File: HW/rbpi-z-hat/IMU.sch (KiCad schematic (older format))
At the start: 11 parts, among them U1 MPU-9250

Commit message: Commit...
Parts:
- removed C1, C5: 100nF, Capacitor_SMD:C_0603_1608Metric, symbol Device:C
- removed C3: 10nF, Capacitor_SMD:C_0603_1608Metric, symbol Device:C
- removed C6: 22uF/10V, Capacitor_SMD:C_1206_3216Metric, symbol Device:C
- removed C7: 0.1uF, Capacitor_SMD:C_0603_1608Metric, symbol Device:C
- removed L1, L4: Ferrite_Bead, Inductor_SMD:L_0603_1608Metric, symbol Device:Ferrite_Bead
- removed R1: 120, Resistor_SMD:R_0603_1608Metric, symbol Device:R
- removed R2, R3: 10K, Resistor_SMD:R_0603_1608Metric, symbol Device:R
- removed U1: MPU-9250, Package_DFN_QFN:QFN-24-1EP_3x3mm_P0.4mm_EP1.75x1.6mm, symbol Sensor_Motion:MPU-9250
- added C22: 100nF, Capacitor_SMD:C_0603_1608Metric, symbol Device:C
- added L10, L11: Ferrite_Bead, Inductor_SMD:L_0603_1608Metric, symbol Device:Ferrite_Bead
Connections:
- new net IMU_FGND: L11.2
- new net IMU_GND: C22.2, L11.1
- new net IMU_VIN: C22.1, L10.1
- new net MIC5504_IMU/MIC_VIN: L10.2
- no-connect marks 2 -> 0
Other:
- note removed: "CL31B226KPHNNNE"

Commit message: Commit
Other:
- moved on the sheet: C22, L10, L11
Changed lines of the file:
@@
 L Device:Ferrite_Bead L?
 U 1 1 5EE0B780
-P 3850 6650
+P 3550 6650
 AR Path="/5ED663F7/5EE0B780" Ref="L?"  Part="1"
 AR Path="/5EF65A4D/5EF663FB/5EE0B780" Ref="L?"  Part="1"
 AR Path="/5EF65A4D/5EE0B780" Ref="L?"  Part="1"
 AR Path="/5EE06F22/5EE0B780" Ref="L10"  Part="1"
-F 0 "L10" V 4100 6650 50  0000 C CNN
-F 1 "Ferrite_Bead" V 4000 6650 50  0000 C CNN
-F 2 "Inductor_SMD:L_0603_1608Metric" V 3780 6650 50  0001 C CNN
-F 3 "~" H 3850 6650 50  0001 C CNN
-	1    3850 6650
+F 0 "L10" V 3800 6650 50  0000 C CNN
+F 1 "Ferrite_Bead" V 3700 6650 50  0000 C CNN
+F 2 "Inductor_SMD:L_0603_1608Metric" V 3480 6650 50  0001 C CNN
+F 3 "~" H 3550 6650 50  0001 C CNN
+	1    3550 6650
 	0    -1   -1   0
 $EndComp
@@
 L Device:C C?
 U 1 1 5EE0B786
-P 3500 7200
+P 3200 7200
 AR Path="/5ED663F7/5EE0B786" Ref="C?"  Part="1"
 AR Path="/5EF65A4D/5EF663FB/5EE0B786" Ref="C?"  Part="1"
 AR Path="/5EF65A4D/5EE0B786" Ref="C?"  Part="1"
 AR Path="/5EE06F22/5EE0B786" Ref="C22"  Part="1"
-F 0 "C22" H 3550 7300 50  0000 L CNN
-F 1 "100nF" H 3550 7100 50  0000 L CNN
-F 2 "Capacitor_SMD:C_0603_1608Metric" H 3538 7050 50  0001 C CNN
-F 3 "" H 3500 7200 50  0001 C CNN
-	1    3500 7200
+F 0 "C22" H 3250 7300 50  0000 L CNN
+F 1 "100nF" H 3250 7100 50  0000 L CNN
+F 2 "Capacitor_SMD:C_0603_1608Metric" H 3238 7050 50  0001 C CNN
+F 3 "" H 3200 7200 50  0001 C CNN
+	1    3200 7200
 	1    0    0    -1
 $EndComp
 Wire Wire Line
-	3250 6650 3500 6650
-Wire Wire Line
-	3700 6650 3500 6650
-Connection ~ 3500 6650
-Wire Wire Line
-	3500 6650 3500 7050
-Wire Wire Line
-	3500 7350 3500 7750
+	2950 6650 3200 6650
+Wire Wire Line
+	3400 6650 3200 6650
+Connection ~ 3200 6650
+Wire Wire Line
+	3200 6650 3200 7050
+Wire Wire Line
+	3200 7350 3200 7750
 $Comp
 L Device:Ferrite_Bead L?
 U 1 1 5EE0B798
-P 3850 7750
+P 3550 7750
 AR Path="/5ED663F7/5EE0B798" Ref="L?"  Part="1"
 AR Path="/5EF65A4D/5EF663FB/5EE0B798" Ref="L?"  Part="1"
 AR Path="/5EF65A4D/5EE0B798" Ref="L?"  Part="1"
 AR Path="/5EE06F22/5EE0B798" Ref="L11"  Part="1"
-F 0 "L11" V 4050 7750 50  0000 C CNN
-F 1 "Ferrite_Bead" V 3700 7750 50  0000 C CNN
-F 2 "Inductor_SMD:L_0603_1608Metric" V 3780 7750 50  0001 C CNN
-F 3 "~" H 3850 7750 50  0001 C CNN
-	1    3850 7750
+F 0 "L11" V 3750 7750 50  0000 C CNN
+F 1 "Ferrite_Bead" V 3400 7750 50  0000 C CNN
+F 2 "Inductor_SMD:L_0603_1608Metric" V 3480 7750 50  0001 C CNN
+F 3 "~" H 3550 7750 50  0001 C CNN
+	1    3550 7750
 	0    -1   -1   0
 $EndComp
 Wire Wire Line
-	3700 7750 3500 7750
-Connection ~ 3500 7750
-Wire Wire Line
-	3500 7750 3250 7750
+	3400 7750 3200 7750
+Connection ~ 3200 7750
+Wire Wire Line
+	3200 7750 2950 7750
 Text Label 5550 6650 2    50   ~ 0
 IMU_VDD
@@
 IMU_VDD
 Wire Wire Line
-	4000 6650 4200 6650
-Wire Wire Line
-	4000 7750 4550 7750
-Text HLabel 3250 6650 0    50   Input ~ 0
+	3700 6650 4200 6650
+Wire Wire Line
+	3700 7750 4150 7750
+Text HLabel 2950 6650 0    50   Input ~ 0
 IMU_VIN
-Text HLabel 3250 7750 0    50   Input ~ 0
+Text HLabel 2950 7750 0    50   Input ~ 0
 IMU_GND
 Wire Wire Line
@@
 Text HLabel 2850 4100 0    50   Input ~ 0
 MPU_INT
+Wire Wire Line
+	4150 7750 4150 6850
+Wire Wire Line
+	4150 6850 4200 6850
+Connection ~ 4150 7750
+Wire Wire Line
+	4150 7750 4550 7750
+Wire Wire Line
+	4200 2650 4050 2650
+Wire Wire Line
+	4200 2750 4050 2750
+Wire Wire Line
+	4200 2850 4050 2850
+Wire Wire Line
+	4200 2950 4050 2950
+Wire Wire Line
+	4200 3050 4050 3050
+Wire Wire Line
+	4200 5200 3750 5200
+Wire Wire Line
+	4200 5300 3750 5300
+Text HLabel 3750 5200 0    50   Output ~ 0
+ICM_INT1
+Text HLabel 3750 5300 0    50   Output ~ 0
+ICM_INT2
+Text HLabel 4050 2650 0    50   Output ~ 0
+LSM_DEN
+Text HLabel 4050 2750 0    50   Output ~ 0
+LSM_INT1
+Text HLabel 4050 2850 0    50   Output ~ 0
+LSM_INT2
+Text HLabel 4050 2950 0    50   Output ~ 0
+LSM_INT3
+Text HLabel 4050 3050 0    50   Output ~ 0
+LSM_INT4
+Wire Wire Line
+	4200 6750 4150 6750
+Text HLabel 4150 6750 0    50   Input ~ 0
+SENS_EN
 $EndSCHEMATC

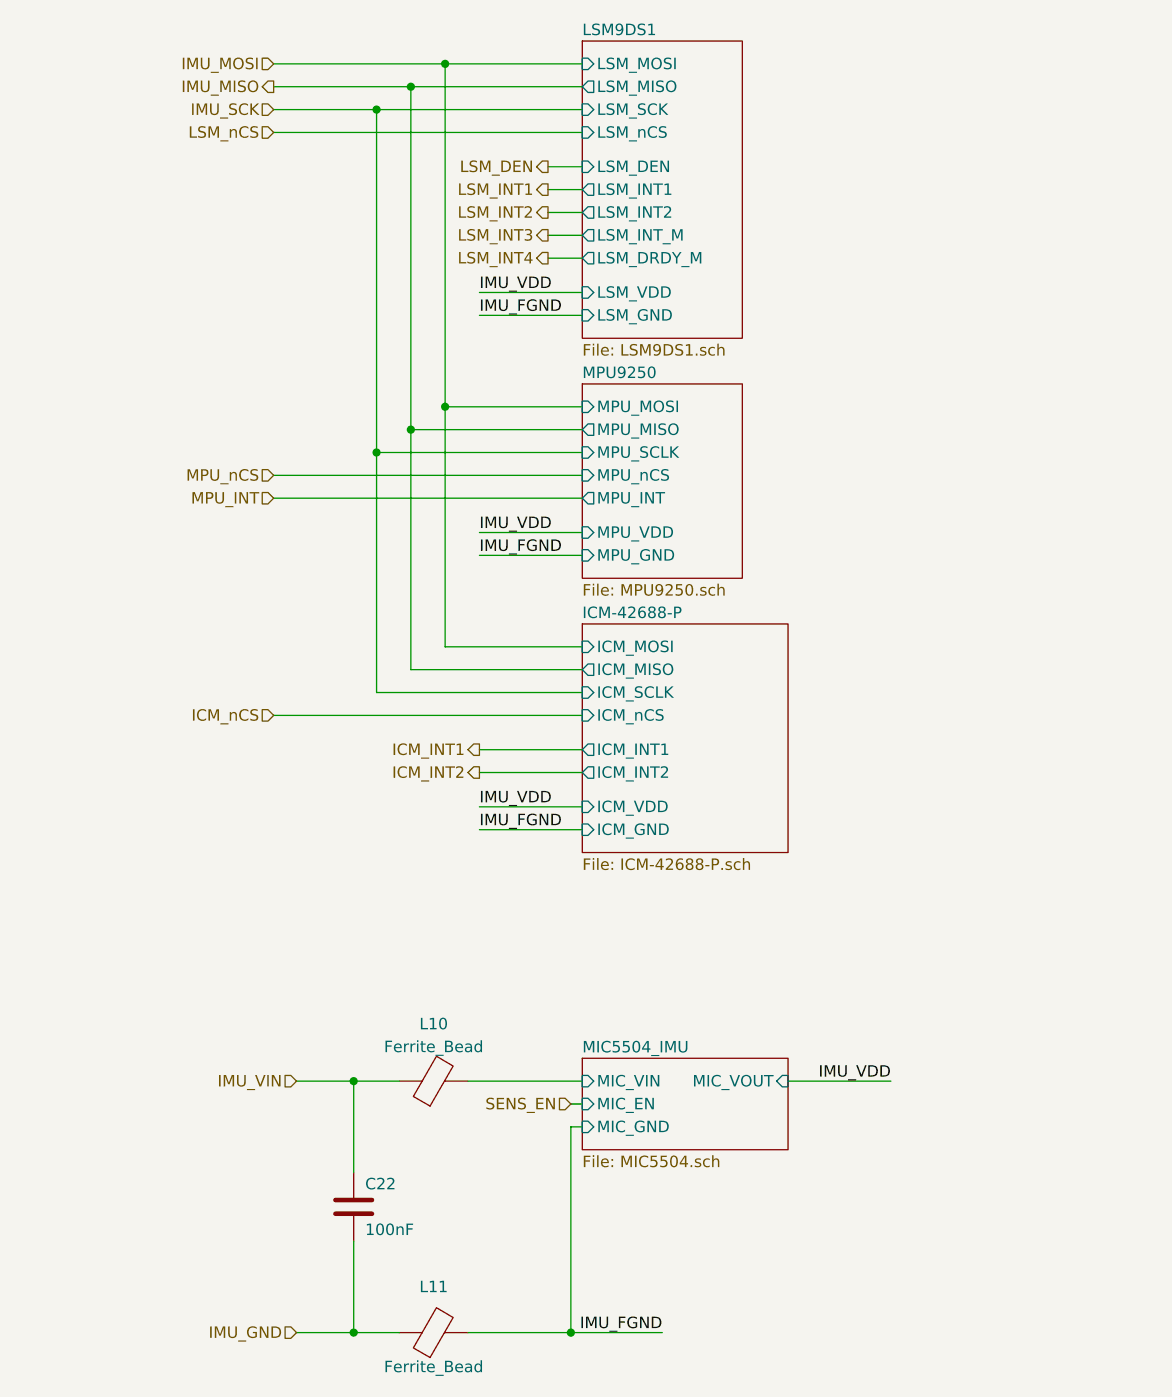
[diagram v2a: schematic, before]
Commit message: Removed MPU-9250
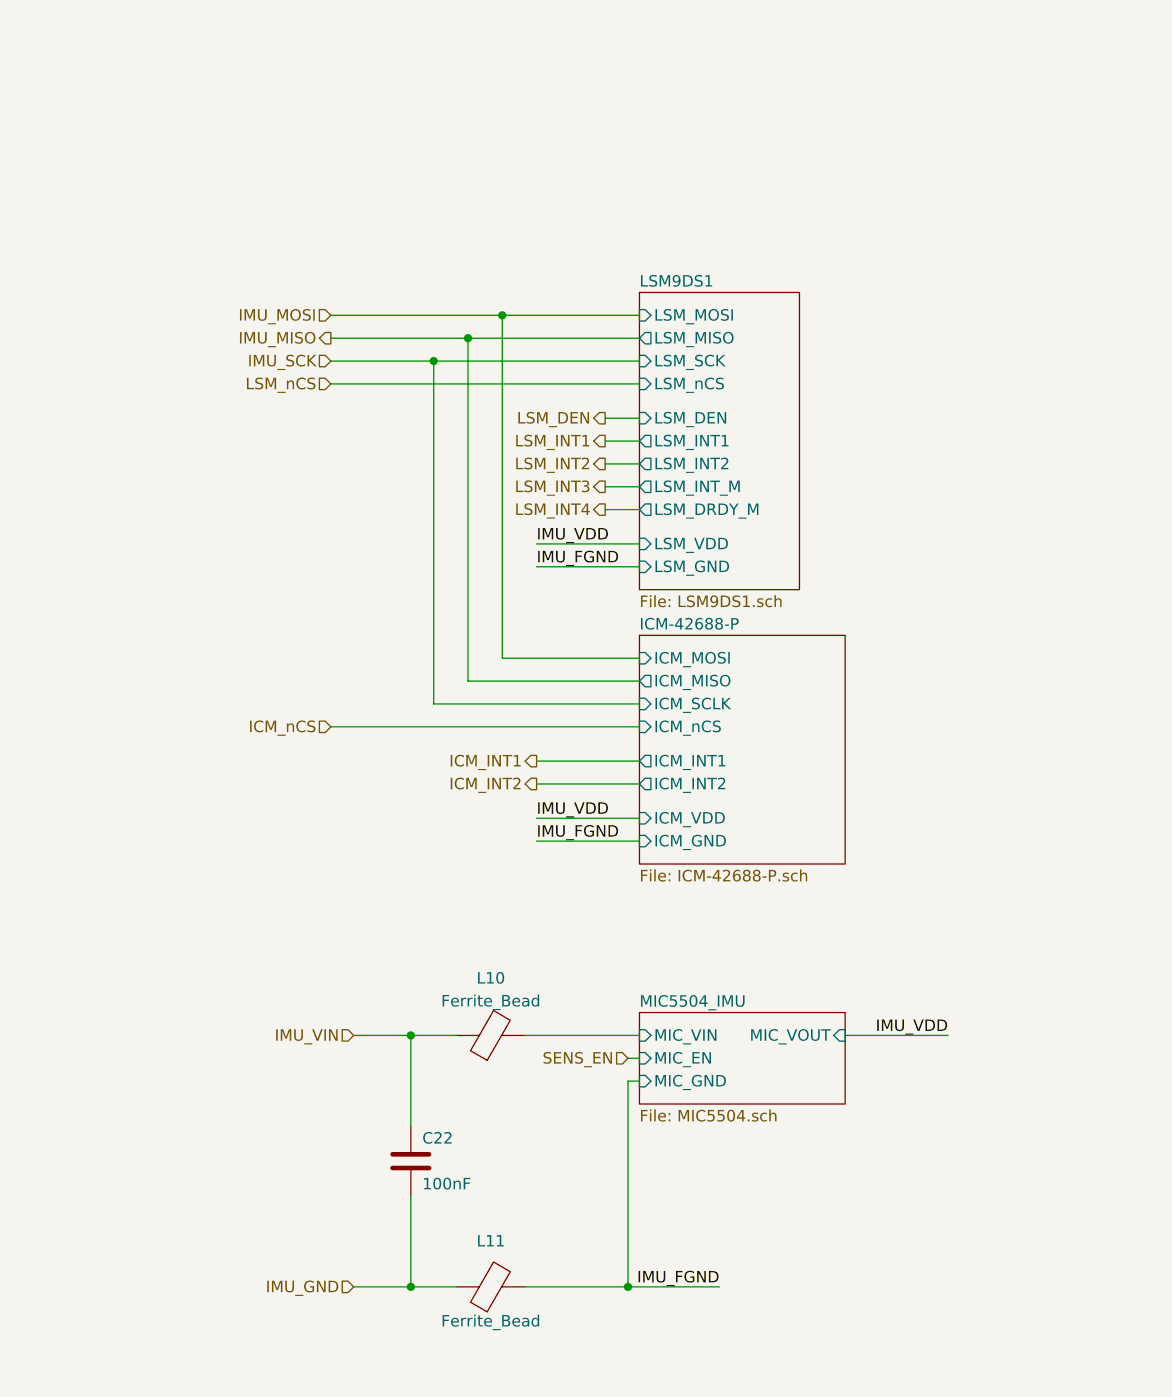
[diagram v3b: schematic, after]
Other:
- moved on the sheet: C22, L10, L11

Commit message: Commit
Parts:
- removed C22: 100nF, Capacitor_SMD:C_0603_1608Metric, symbol Device:C
- removed L10, L11: Ferrite_Bead, Inductor_SMD:L_0603_1608Metric, symbol Device:Ferrite_Bead
- added C?: 22uF/10V, Capacitor_SMD:C_1206_3216Metric, symbol Device:C
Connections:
- net IMU_GND: now also C?.2
- net IMU_VIN: now also C?.1
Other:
- note added: "CL31B226KPHNNNE"
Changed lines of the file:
@@
 $Descr A4 8268 11693 portrait
 encoding utf-8
-Sheet 14 17
+Sheet 13 17
 Title ""
 Date ""
@@
 $EndSheet
 Wire Wire Line
-	5800 6450 5350 6450
-$Comp
-L Device:Ferrite_Bead L?
-U 1 1 5EE0B780
-P 3800 6450
-AR Path="/5ED663F7/5EE0B780" Ref="L?"  Part="1"
-AR Path="/5EF65A4D/5EF663FB/5EE0B780" Ref="L?"  Part="1"
-AR Path="/5EF65A4D/5EE0B780" Ref="L?"  Part="1"
-AR Path="/5EE06F22/5EE0B780" Ref="L10"  Part="1"
-F 0 "L10" V 4050 6450 50  0000 C CNN
-F 1 "Ferrite_Bead" V 3950 6450 50  0000 C CNN
-F 2 "Inductor_SMD:L_0603_1608Metric" V 3730 6450 50  0001 C CNN
-F 3 "~" H 3800 6450 50  0001 C CNN
-	1    3800 6450
-	0    -1   -1   0
-$EndComp
-$Comp
-L Device:C C?
-U 1 1 5EE0B786
-P 3450 7000
-AR Path="/5ED663F7/5EE0B786" Ref="C?"  Part="1"
-AR Path="/5EF65A4D/5EF663FB/5EE0B786" Ref="C?"  Part="1"
-AR Path="/5EF65A4D/5EE0B786" Ref="C?"  Part="1"
-AR Path="/5EE06F22/5EE0B786" Ref="C22"  Part="1"
-F 0 "C22" H 3500 7100 50  0000 L CNN
-F 1 "100nF" H 3500 6900 50  0000 L CNN
-F 2 "Capacitor_SMD:C_0603_1608Metric" H 3488 6850 50  0001 C CNN
-F 3 "" H 3450 7000 50  0001 C CNN
-	1    3450 7000
-	1    0    0    -1
-$EndComp
-Wire Wire Line
-	3200 6450 3450 6450
-Wire Wire Line
-	3650 6450 3450 6450
-Connection ~ 3450 6450
-Wire Wire Line
-	3450 6450 3450 6850
-Wire Wire Line
-	3450 7150 3450 7550
-$Comp
-L Device:Ferrite_Bead L?
-U 1 1 5EE0B798
-P 3800 7550
-AR Path="/5ED663F7/5EE0B798" Ref="L?"  Part="1"
-AR Path="/5EF65A4D/5EF663FB/5EE0B798" Ref="L?"  Part="1"
-AR Path="/5EF65A4D/5EE0B798" Ref="L?"  Part="1"
-AR Path="/5EE06F22/5EE0B798" Ref="L11"  Part="1"
-F 0 "L11" V 4000 7550 50  0000 C CNN
-F 1 "Ferrite_Bead" V 3650 7550 50  0000 C CNN
-F 2 "Inductor_SMD:L_0603_1608Metric" V 3730 7550 50  0001 C CNN
-F 3 "~" H 3800 7550 50  0001 C CNN
-	1    3800 7550
-	0    -1   -1   0
-$EndComp
-Wire Wire Line
-	3650 7550 3450 7550
-Connection ~ 3450 7550
-Wire Wire Line
-	3450 7550 3200 7550
-Text Label 5800 6450 2    50   ~ 0
-IMU_VDD
-Text Label 4800 7550 2    50   ~ 0
-IMU_FGND
-$Sheet
-S 4450 6350 900  400
-U 5EE2A025
-F0 "MIC5504_IMU" 50
-F1 "MIC5504.sch" 50
-F2 "MIC_EN" I L 4450 6550 50
-F3 "MIC_VIN" I L 4450 6450 50
-F4 "MIC_VOUT" I R 5350 6450 50
-F5 "MIC_GND" I L 4450 6650 50
-$EndSheet
-Wire Wire Line
 	4000 5600 4450 5600
 Text Label 4000 5600 0    50   ~ 0
@@
 Text Label 4000 5500 0    50   ~ 0
 IMU_VDD
-Wire Wire Line
-	3950 6450 4450 6450
-Wire Wire Line
-	3950 7550 4400 7550
-Text HLabel 3200 6450 0    50   Input ~ 0
-IMU_VIN
-Text HLabel 3200 7550 0    50   Input ~ 0
-IMU_GND
 Wire Wire Line
 	4000 4400 4450 4400
@@
 ICM_nCS
 Wire Wire Line
-	4400 7550 4400 6650
-Wire Wire Line
-	4400 6650 4450 6650
-Connection ~ 4400 7550
-Wire Wire Line
-	4400 7550 4800 7550
-Wire Wire Line
 	4450 3750 4300 3750
 Wire Wire Line
@@
 LSM_INT4
 Wire Wire Line
-	4450 6550 4400 6550
-Text HLabel 4400 6550 0    50   Input ~ 0
-SENS_EN
-Wire Wire Line
 	3850 3300 3850 4800
 Wire Wire Line
@@
 Wire Wire Line
 	3550 3500 3550 5000
+Wire Wire Line
+	3600 6400 3600 6650
+Wire Wire Line
+	3600 7200 3600 6950
+$Comp
+L Device:C C?
+U 1 1 5EE70328
+P 3600 6800
+AR Path="/5ED663F7/5EE70328" Ref="C?"  Part="1"
+AR Path="/5EF65A4D/5EF663FB/5EE70328" Ref="C?"  Part="1"
+AR Path="/5EF65A4D/5EE70328" Ref="C?"  Part="1"
+AR Path="/5EDADA57/5EE70328" Ref="C?"  Part="1"
+AR Path="/5EF65A4D/5EE0D50D/5EE70328" Ref="C?"  Part="1"
+AR Path="/5EE06F22/5EE2A025/5EE70328" Ref="C?"  Part="1"
+AR Path="/5EE06F22/5EE70328" Ref="C?"  Part="1"
+F 0 "C?" H 3450 6900 50  0000 L CNN
+F 1 "22uF/10V" H 3200 6700 50  0000 L CNN
+F 2 "Capacitor_SMD:C_1206_3216Metric" H 3638 6650 50  0001 C CNN
+F 3 "" H 3600 6800 50  0001 C CNN
+F 4 "https://www.terraelectronica.ru/product/1641498" H 3600 6800 50  0001 C CNN "URL"
+	1    3600 6800
+	-1   0    0    -1
+$EndComp
+Text Notes 3500 7200 1    50   ~ 0
+CL31B226KPHNNNE
+Connection ~ 3600 6400
+Text HLabel 3100 6400 0    50   Input ~ 0
+IMU_VIN
+Wire Wire Line
+	3100 6400 3600 6400
+Text HLabel 3100 7200 0    50   Input ~ 0
+IMU_GND
+Wire Wire Line
+	3100 7200 3600 7200
+Text Label 4250 6400 2    50   ~ 0
+IMU_VDD
+Wire Wire Line
+	3600 6400 4250 6400
+Text Label 4250 7200 2    50   ~ 0
+IMU_FGND
+Wire Wire Line
+	3600 7200 4250 7200
+Connection ~ 3600 7200
 $EndSCHEMATC

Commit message: Commit
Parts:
- gave numbers to parts that had none: 1
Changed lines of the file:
@@
 AR Path="/5EF65A4D/5EE0D50D/5EE70328" Ref="C?"  Part="1"
 AR Path="/5EE06F22/5EE2A025/5EE70328" Ref="C?"  Part="1"
-AR Path="/5EE06F22/5EE70328" Ref="C?"  Part="1"
-F 0 "C?" H 3450 6900 50  0000 L CNN
+AR Path="/5EE06F22/5EE70328" Ref="C3"  Part="1"
+F 0 "C3" H 3450 6900 50  0000 L CNN
 F 1 "22uF/10V" H 3200 6700 50  0000 L CNN
 F 2 "Capacitor_SMD:C_1206_3216Metric" H 3638 6650 50  0001 C CNN

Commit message: Changes in Schematics
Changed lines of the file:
@@
 $Descr A4 8268 11693 portrait
 encoding utf-8
-Sheet 13 17
+Sheet 12 17
 Title "RasPi Zero NAV Hat"
 Date "2020-08-11"
@@
 Text HLabel 4000 5350 0    50   Output ~ 0
 ICM_INT2
-Text HLabel 4300 3750 0    50   Output ~ 0
+Text HLabel 4300 3750 0    50   Input ~ 0
 LSM_DEN
 Text HLabel 4300 3850 0    50   Output ~ 0
